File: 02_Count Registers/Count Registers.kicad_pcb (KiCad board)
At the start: 2 copper layers, 100 x 100 mm, 54 parts, among them J1 Data bus, J2 Alu-X bus, J3 Alu-Y bus, J4 Input 1, J5 Input 2, U1 74LS139, U10 74LS245, U11 74LS245, U12 74LS245, U13 74LS245, U2 74LS04, U3 74LS08, U4 74LS193, U5 74LS245, U6 74LS193, U7 74LS193, U8 74LS245, U9 74LS193

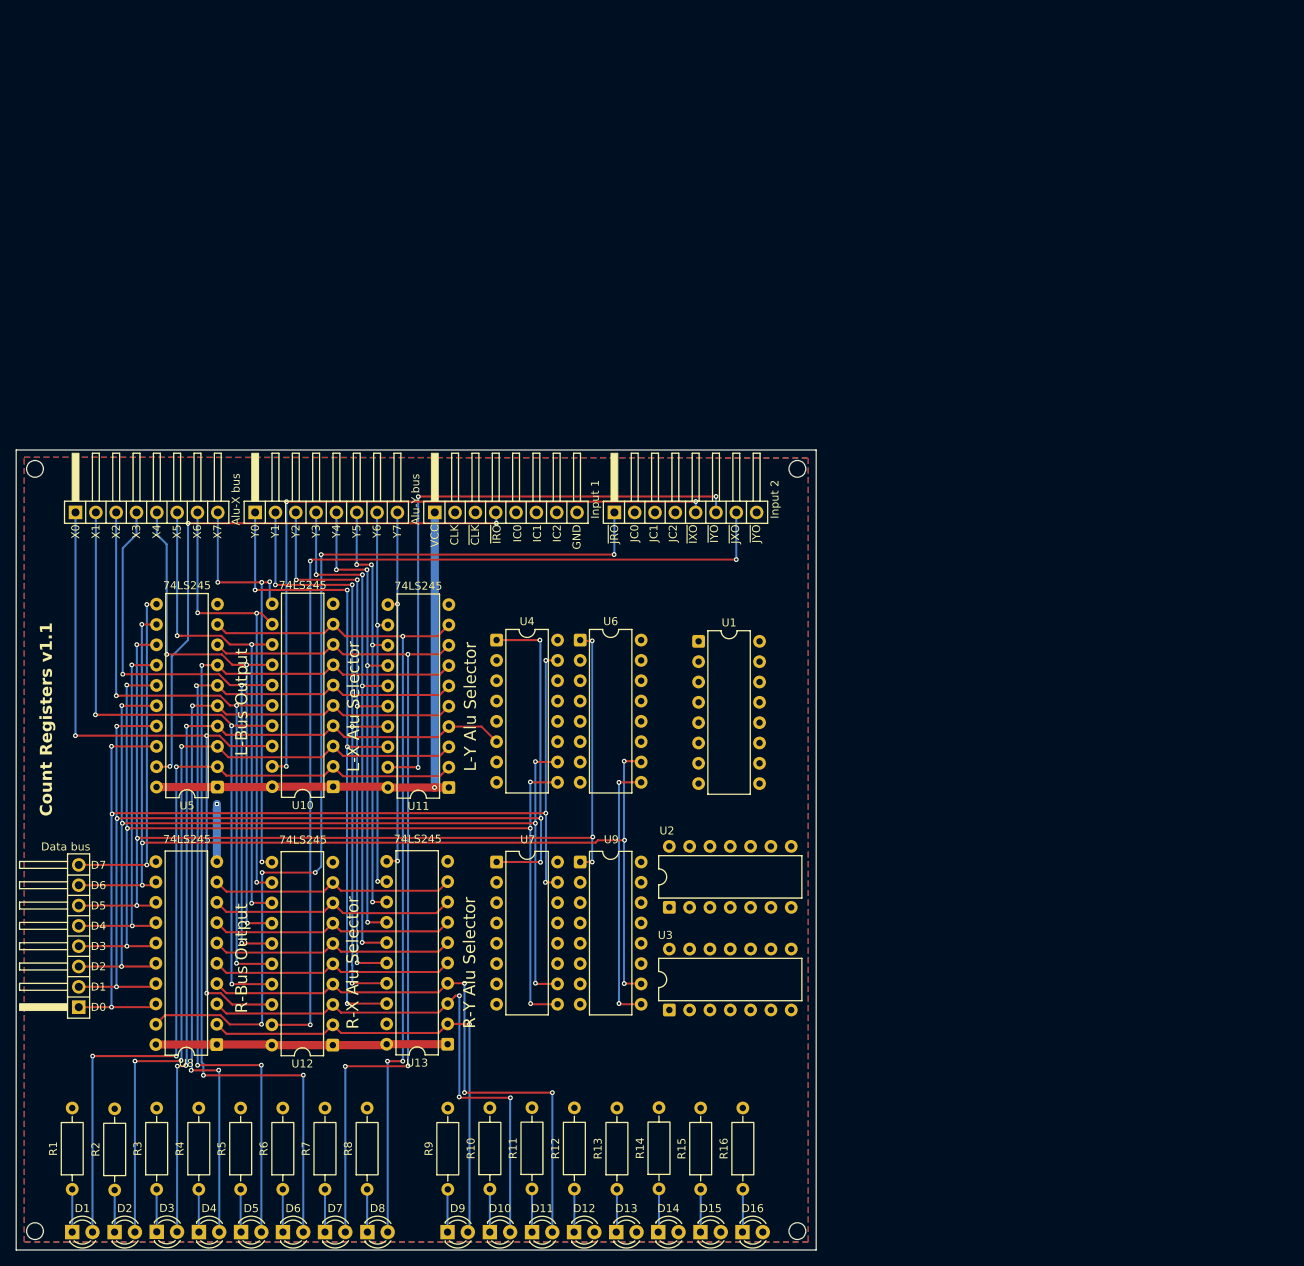
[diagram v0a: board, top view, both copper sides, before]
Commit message: Last revision of the cpu, all boards have been ordered. Implementation to be tested and documented in following commits.
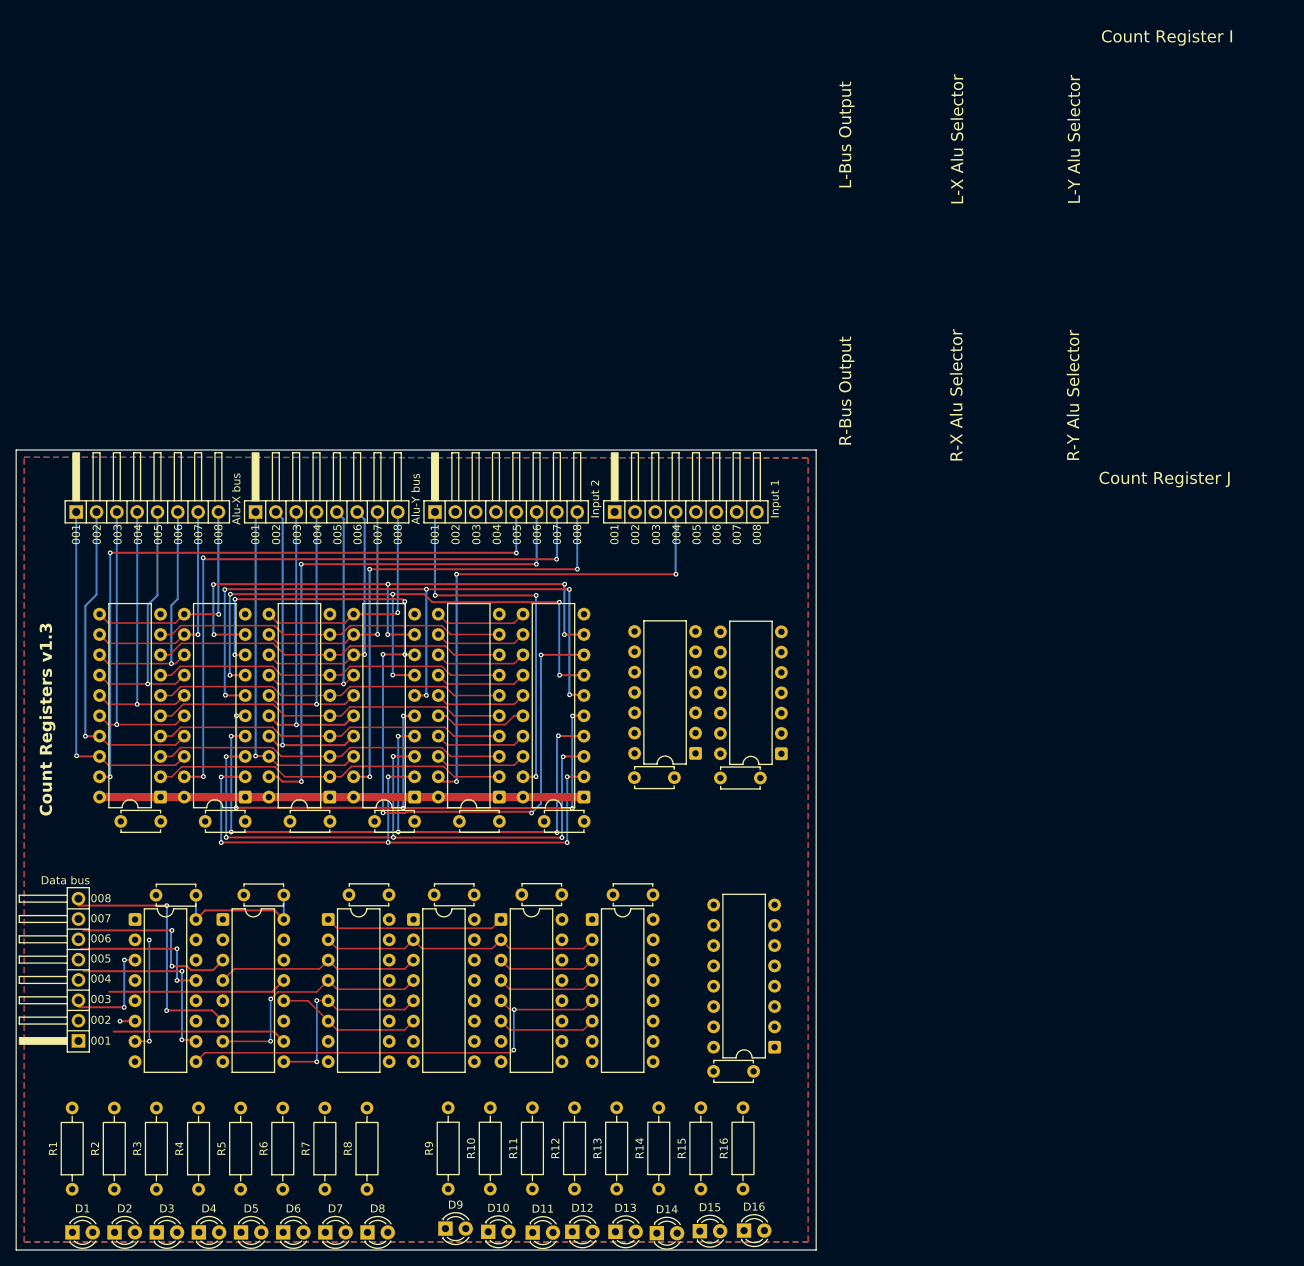
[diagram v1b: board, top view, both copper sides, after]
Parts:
- removed REF** (x4): MountingHole_2.1mm, MountingHole:MountingHole_2.1mm
- added C1: 100nF, Capacitor_THT:C_Disc_D4.7mm_W2.5mm_P5.00mm, F.Cu at (107.3, 71.0)
- added C10: 10nF, Capacitor_THT:C_Disc_D4.7mm_W2.5mm_P5.00mm, F.Cu at (48.1, 76.4)
- added C11: 10nF, Capacitor_THT:C_Disc_D4.7mm_W2.5mm_P5.00mm, F.Cu at (69.2, 76.4)
- added C12: 10nF, Capacitor_THT:C_Disc_D4.7mm_W2.5mm_P5.00mm, F.Cu at (58.6, 76.4)
- added C13: 10nF, Capacitor_THT:C_Disc_D4.7mm_W2.5mm_P5.00mm, F.Cu at (79.8, 76.4)
- added C14: 10nF, Capacitor_THT:C_Disc_D4.7mm_W2.5mm_P5.00mm, F.Cu at (52.5, 85.7)
- added C15: 10nF, Capacitor_THT:C_Disc_D4.7mm_W2.5mm_P5.00mm, F.Cu at (63.5, 85.6)
- added C2: 100nF, Capacitor_THT:C_Disc_D4.7mm_W2.5mm_P5.00mm, F.Cu at (117.2, 107.7)
- added C3: 100nF, Capacitor_THT:C_Disc_D4.7mm_W2.5mm_P5.00mm, F.Cu at (118.0, 71.0)
- added C4: 10nF, Capacitor_THT:C_Disc_D4.7mm_W2.5mm_P5.00mm, F.Cu at (98.2, 85.6)
- added C5: 10nF, Capacitor_THT:C_Disc_D4.7mm_W2.5mm_P5.00mm, F.Cu at (90.4, 76.4)
- added C6: 10nF, Capacitor_THT:C_Disc_D4.7mm_W2.5mm_P5.00mm, F.Cu at (76.6, 85.6)
- added C7: 10nF, Capacitor_THT:C_Disc_D4.7mm_W2.5mm_P5.00mm, F.Cu at (109.6, 85.6)
- added C8: 10nF, Capacitor_THT:C_Disc_D4.7mm_W2.5mm_P5.00mm, F.Cu at (101.0, 76.4)
- added C9: 10nF, Capacitor_THT:C_Disc_D4.7mm_W2.5mm_P5.00mm, F.Cu at (87.2, 85.6)
- added U14: 74LS157, Package_DIP:DIP-16_W7.62mm, F.Cu at (44.9, 88.7)
- added U15: 74LS157, Package_DIP:DIP-16_W7.62mm, F.Cu at (55.8, 88.7)
- U1: value 74LS139 -> 74LS08; footprint Package_DIP:DIP-16_W7.62mm -> Package_DIP:DIP-14_W7.62mm
- U2: value 74LS04 -> 74LS139; footprint Package_DIP:DIP-14_W7.62mm -> Package_DIP:DIP-16_W7.62mm
- U4, U6, U7, U9: value 74LS193 -> 74LS169
- moved U8 55.3 mm to (101.0, 73.4)
- moved U6 47.0 mm to (69.0, 88.7)
- moved U5 35.2 mm to (90.4, 73.4)
- moved U3 35.0 mm to (125.7, 68.0), turned to 180 degrees
- moved U4 34.9 mm to (90.6, 88.7)
- moved U12 32.9 mm to (58.6, 73.4)
- moved U13 31.2 mm to (79.8, 73.4)
- moved J4 22.5 mm to (104.8, 40.5)
- moved J5 22.4 mm to (82.3, 40.5)
- moved U9 22.0 mm to (79.7, 88.7)
- moved U2 21.9 mm to (124.8, 104.7), turned to 180 degrees
- moved U10 21.6 mm to (48.0, 73.4)
- moved U11 14.9 mm to (69.2, 73.4)
- moved U1 14.0 mm to (114.9, 67.9), turned to 180 degrees
- moved U7 13.9 mm to (102.0, 88.7)
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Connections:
- net /X0 renamed X0
- net /X1 renamed X1
- net /X2 renamed X2
- net /X3 renamed X3
- net /X4 renamed X4
- net /X5 renamed X5
- net /X6 renamed X6
- net /X7 renamed X7
- net /Y0 renamed Y0
- net /Y1 renamed Y1
- net /Y2 renamed Y2
- net /Y3 renamed Y3
- net /Y4 renamed Y4
- net /Y5 renamed Y5
- net /Y6 renamed Y6
- net /Y7 renamed Y7
- net /~{CLK} renamed ~{CLK}
- net /~{IRO} renamed ~{IRO}
- net /~{IXO} renamed ~{IXO}
- net /~{IYO} renamed ~{IYO}
- net /~{JRO} renamed ~{JRO}
- net /~{JXO} renamed ~{JXO}
- net /~{JYO} renamed ~{JYO}
- J1 pad 1: /D0 -> D0
- J1 pad 2: /D1 -> D1
- J1 pad 3: /D2 -> D2
- J1 pad 4: /D3 -> D3
- J1 pad 5: /D4 -> D4
- J1 pad 6: /D5 -> D5
- J1 pad 7: /D6 -> D6
- J1 pad 8: /D7 -> D7
- J4 pad 1: /VCC -> VCC
- J4 pad 2: /CLK -> CLK
- J4 pad 5: /IC0 -> ~{IRI}
- J4 pad 6: /IC1 -> IC0
- J4 pad 7: /IC2 -> IC1
- J4 pad 8: /GND -> GND
- J5 pad 2: /JC0 -> ~{JRI}
- J5 pad 3: /JC1 -> JC0
- J5 pad 4: /JC2 -> JC1
- R1 pad 2: /GND -> GND
- R10 pad 2: /GND -> GND
- R11 pad 2: /GND -> GND
- R12 pad 2: /GND -> GND
- R13 pad 2: /GND -> GND
- R14 pad 2: /GND -> GND
- R15 pad 2: /GND -> GND
- R16 pad 2: /GND -> GND
- R2 pad 2: /GND -> GND
- R3 pad 2: /GND -> GND
- R4 pad 2: /GND -> GND
- R5 pad 2: /GND -> GND
- R6 pad 2: /GND -> GND
- R7 pad 2: /GND -> GND
- R8 pad 2: /GND -> GND
- R9 pad 2: /GND -> GND
- U1 pad 1: /GND -> ~{IRI}
- U1 pad 10: Net-(U1B-O2) -> /Count register J/U/~{D}
- U1 pad 11: Net-(U1B-O1) -> /Count register J/~{WE}
- U1 pad 12: unconnected-(U1B-O0-Pad12) -> ~{JRI}
- U1 pad 13: /JC0 -> Net-(U2B-O3)
- U1 pad 14: /JC1 -> VCC
- U1 pad 2: /IC1 -> Net-(U2A-O3)
- U1 pad 3: /IC0 -> /Count register I/~{WE}
- U1 pad 4: unconnected-(U1A-O0-Pad4) -> Net-(U2A-O1)
- U1 pad 5: Net-(U1A-O1) -> /Count register I/U/~{D}
- U1 pad 6: Net-(U1A-O2) -> /Count register I/~{CE}
- U1 pad 7: /Count register I/~{WE} -> GND
- U1 pad 8: /GND -> /Count register J/~{CE}
- U1 pad 9: /Count register J/~{WE} -> Net-(U2B-O1)
- U10 pad 1: /VCC -> VCC
- U10 pad 10: /GND -> GND
- U10 pad 20: /VCC -> VCC
- U11 pad 1: /VCC -> VCC
- U11 pad 10: /GND -> GND
- U11 pad 20: /VCC -> VCC
- U12 pad 1: /VCC -> VCC
- U12 pad 10: /GND -> GND
- U12 pad 20: /VCC -> VCC
- U13 pad 1: /VCC -> VCC
- U13 pad 10: /GND -> GND
- U13 pad 20: /VCC -> VCC
- U2 pad 1: Net-(U1A-O1) -> GND
- U2 pad 10: Net-(U2-Pad10) -> /Count register J/U/~{D}
- U2 pad 11: Net-(U1B-O2) -> Net-(U2B-O1)
- U2 pad 12: (no net) -> unconnected-(U2B-O0-Pad12)
- U2 pad 13: (no net) -> JC1
- U2 pad 14: /VCC -> JC0
- U2 pad 2: Net-(U2-Pad2) -> IC0
- U2 pad 3: Net-(U1A-O2) -> IC1
- U2 pad 4: Net-(U2-Pad4) -> unconnected-(U2A-O0-Pad4)
- U2 pad 5: (no net) -> Net-(U2A-O1)
- U2 pad 6: (no net) -> /Count register I/U/~{D}
- U2 pad 7: /GND -> Net-(U2A-O3)
- U2 pad 8: Net-(U2-Pad8) -> GND
- U2 pad 9: Net-(U1B-O1) -> Net-(U2B-O3)
- U3 pad 1: Net-(U2-Pad2) -> Net-(U2B-O3)
- U3 pad 10: /CLK -> GND
- U3 pad 11: /Count register J/DOWN -> unconnected-(U3-Pad11)
- U3 pad 12: Net-(U2-Pad10) -> GND
- U3 pad 13: /CLK -> GND
- U3 pad 14: /VCC -> VCC
- U3 pad 2: /CLK -> Net-(U2A-O3)
- U3 pad 3: /Count register I/UP -> /Word Selector/~{CLR}
- U3 pad 4: Net-(U2-Pad4) -> GND
- U3 pad 5: /CLK -> GND
- U3 pad 6: /Count register I/DOWN -> unconnected-(U3-Pad6)
- U3 pad 7: /GND -> GND
- U3 pad 8: /Count register J/UP -> unconnected-(U3-Pad8)
- U3 pad 9: Net-(U2-Pad8) -> GND
- U4 pad 1: /D1 -> /Count register I/U/~{D}
- U4 pad 10: /D2 -> GND
- U4 pad 11: /Count register I/~{WE} -> /Alu selector I-X/Q3
- U4 pad 12: Net-(U4-~{CO}) -> /Alu selector I-X/Q2
- U4 pad 13: Net-(U4-~{BO}) -> /Alu selector I-X/Q1
- U4 pad 14: /IC2 -> /Alu selector I-X/Q0
- U4 pad 15: /D0 -> Net-(U4-~{TC})
- U4 pad 16: /VCC -> VCC
- U4 pad 2: /Alu selector I-X/Q1 -> CLK
- U4 pad 3: /Alu selector I-X/Q0 -> S0
- U4 pad 4: /Count register I/DOWN -> S1
- U4 pad 5: /Count register I/UP -> S2
- U4 pad 6: /Alu selector I-X/Q2 -> S3
- U4 pad 7: /Alu selector I-X/Q3 -> /Count register I/~{CE}
- U4 pad 8: /GND -> GND
- U4 pad 9: /D3 -> /Count register I/~{WE}
- U5 pad 1: /VCC -> VCC
- U5 pad 10: /GND -> GND
- U5 pad 11: /D7 -> S7
- U5 pad 12: /D6 -> S6
- U5 pad 13: /D5 -> S5
- U5 pad 14: /D4 -> S4
- U5 pad 15: /D3 -> S3
- U5 pad 16: /D2 -> S2
- U5 pad 17: /D1 -> S1
- U5 pad 18: /D0 -> S0
- U5 pad 20: /VCC -> VCC
- U6 pad 1: /D5 -> /Count register I/U/~{D}
- U6 pad 10: /D6 -> Net-(U4-~{TC})
- U6 pad 11: /Count register I/~{WE} -> /Alu selector I-X/Q7
- U6 pad 12: unconnected-(U6-~{CO}-Pad12) -> /Alu selector I-X/Q6
- U6 pad 13: unconnected-(U6-~{BO}-Pad13) -> /Alu selector I-X/Q5
- U6 pad 14: /IC2 -> /Alu selector I-X/Q4
- U6 pad 15: /D4 -> unconnected-(U6-~{TC}-Pad15)
- U6 pad 16: /VCC -> VCC
- U6 pad 2: /Alu selector I-X/Q5 -> CLK
- U6 pad 3: /Alu selector I-X/Q4 -> S4
- U6 pad 4: Net-(U4-~{BO}) -> S5
- U6 pad 5: Net-(U4-~{CO}) -> S6
- U6 pad 6: /Alu selector I-X/Q6 -> S7
- U6 pad 7: /Alu selector I-X/Q7 -> /Count register I/~{CE}
- U6 pad 8: /GND -> GND
- U6 pad 9: /D7 -> /Count register I/~{WE}
- U7 pad 1: /D1 -> /Count register J/U/~{D}
- U7 pad 10: /D2 -> GND
- U7 pad 11: /Count register J/~{WE} -> /Alu selector J-X/Q3
- U7 pad 12: Net-(U7-~{CO}) -> /Alu selector J-X/Q2
- U7 pad 13: Net-(U7-~{BO}) -> /Alu selector J-X/Q1
- U7 pad 14: /JC2 -> /Alu selector J-X/Q0
- U7 pad 15: /D0 -> Net-(U7-~{TC})
- U7 pad 16: /VCC -> VCC
- U7 pad 2: /Alu selector J-X/Q1 -> CLK
- U7 pad 3: /Alu selector J-X/Q0 -> S0
- U7 pad 4: /Count register J/DOWN -> S1
- U7 pad 5: /Count register J/UP -> S2
- U7 pad 6: /Alu selector J-X/Q2 -> S3
- U7 pad 7: /Alu selector J-X/Q3 -> /Count register J/~{CE}
- U7 pad 8: /GND -> GND
- U7 pad 9: /D3 -> /Count register J/~{WE}
- U8 pad 1: /VCC -> VCC
- U8 pad 10: /GND -> GND
- U8 pad 11: /D7 -> S7
- U8 pad 12: /D6 -> S6
- U8 pad 13: /D5 -> S5
- U8 pad 14: /D4 -> S4
- U8 pad 15: /D3 -> S3
- U8 pad 16: /D2 -> S2
- U8 pad 17: /D1 -> S1
- U8 pad 18: /D0 -> S0
- U8 pad 20: /VCC -> VCC
- U9 pad 1: /D5 -> /Count register J/U/~{D}
- U9 pad 10: /D6 -> Net-(U7-~{TC})
- U9 pad 11: /Count register J/~{WE} -> /Alu selector J-X/Q7
- U9 pad 12: unconnected-(U9-~{CO}-Pad12) -> /Alu selector J-X/Q6
- U9 pad 13: unconnected-(U9-~{BO}-Pad13) -> /Alu selector J-X/Q5
- U9 pad 14: /JC2 -> /Alu selector J-X/Q4
- U9 pad 15: /D4 -> unconnected-(U9-~{TC}-Pad15)
- U9 pad 16: /VCC -> VCC
- U9 pad 2: /Alu selector J-X/Q5 -> CLK
- U9 pad 3: /Alu selector J-X/Q4 -> S4
- U9 pad 4: Net-(U7-~{BO}) -> S5
- U9 pad 5: Net-(U7-~{CO}) -> S6
- U9 pad 6: /Alu selector J-X/Q6 -> S7
- U9 pad 7: /Alu selector J-X/Q7 -> /Count register J/~{CE}
- U9 pad 8: /GND -> GND
- U9 pad 9: /D7 -> /Count register J/~{WE}
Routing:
- net /D1: track 139.3 -> 0.00 mm, vias 6 -> 0
- net /D6: track 136.8 -> 0.00 mm, vias 6 -> 0
- net /D0: track 133.1 -> 0.00 mm, vias 6 -> 0
- net /D5: track 132.6 -> 0.00 mm, vias 6 -> 0
- net /D2: track 131.7 -> 0.00 mm, vias 6 -> 0
- net /D3: track 131.1 -> 0.00 mm, vias 6 -> 0
- net /VCC: track 107.5 -> 0.00 mm, vias 1 -> 0
- net VCC: track 0.00 -> 78.5 mm
- net /D7: track 76.8 -> 0.00 mm, vias 4 -> 0
- net ~{JRO}: track 121.8 -> 47.4 mm, vias 5 -> 3
- net /Alu selector J-X/Q6: track 30.9 -> 104.4 mm, vias 0 -> 8
- net /Alu selector I-X/Q5: track 116.3 -> 44.2 mm, vias 3 -> 0
- net S2: track 0.00 -> 69.2 mm, vias 0 -> 2
- net /Alu selector I-X/Q6: track 110.8 -> 44.4 mm, vias 3 -> 0
- net /Alu selector I-X/Q4: track 109.8 -> 44.2 mm, vias 3 -> 0
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- added copper zone on B.Cu, net GND
- added copper zone on F.Cu, net GND
- removed copper zone on B.Cu, net /GND
- removed copper zone on F.Cu, net /GND
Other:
- board text added: "${REFERENCE}"
- board text added: "Count Register I"
- board text added: "Count Register J"
- board text added: "Count Registers v1.3"
- board text removed: "Count Registers v1.1"
